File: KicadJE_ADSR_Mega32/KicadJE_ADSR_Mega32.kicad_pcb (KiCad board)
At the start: 2 copper layers, 100 x 100 mm, 217 parts, among them J101 ADSR1, J102 ADSR2, J103 ADSR1, J104 ADSR2, J105 ADSR1-G8, J106 ADSR2-G8, J107 ADSR4-G8, J108 ADSR3-G8, J201 AVR-ISP-6, J202 UART, J301 In, J302 +5V reg/doepfer, J303 Out, J304 CV_time, J305 CV doepfer, J401 CV, J402 FM, J403 Trigger, J404 Out, J405 SQ Out, J406 Sine Out, P101 Doepfer_Power_16pin, P302 Doepfer_Power_16pin, P401 Doepfer_Power_16pin, Q301 BC337, Q302 PZT2222A, Q401 UMX1N, Q402 MMBT2222A, Q403 MMBT2222A, Q404 MMBT2222A, Q405 MMBT2222A, SW401 LFO, SW402 SQ_Source, U201 ATmega32A-AU, U301 L78L05_TO92, U302 PT2399, U401 TL074, U402 74HC00, U403 TL072, Y201 16MHz

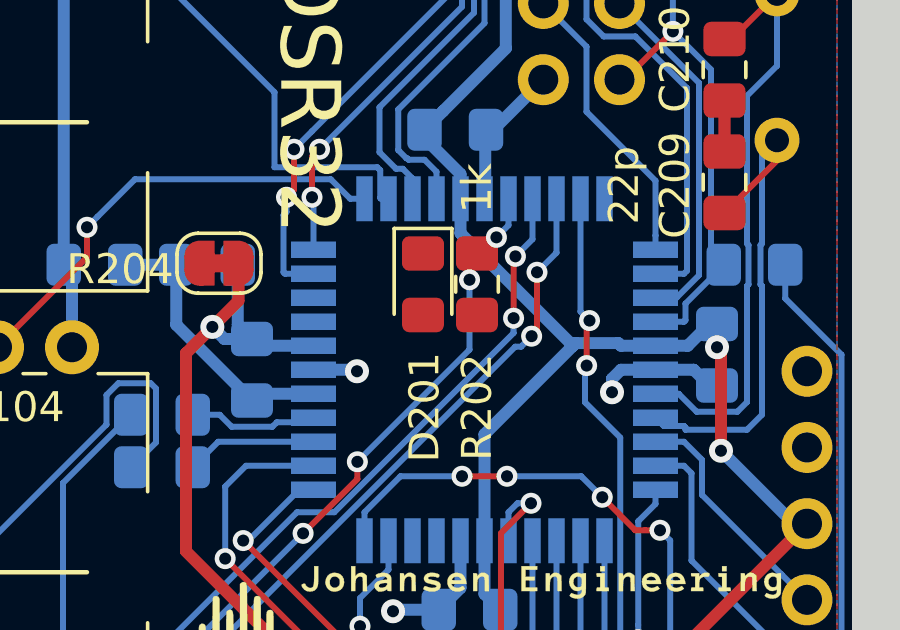
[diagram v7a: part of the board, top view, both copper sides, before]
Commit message: Arduino Blink
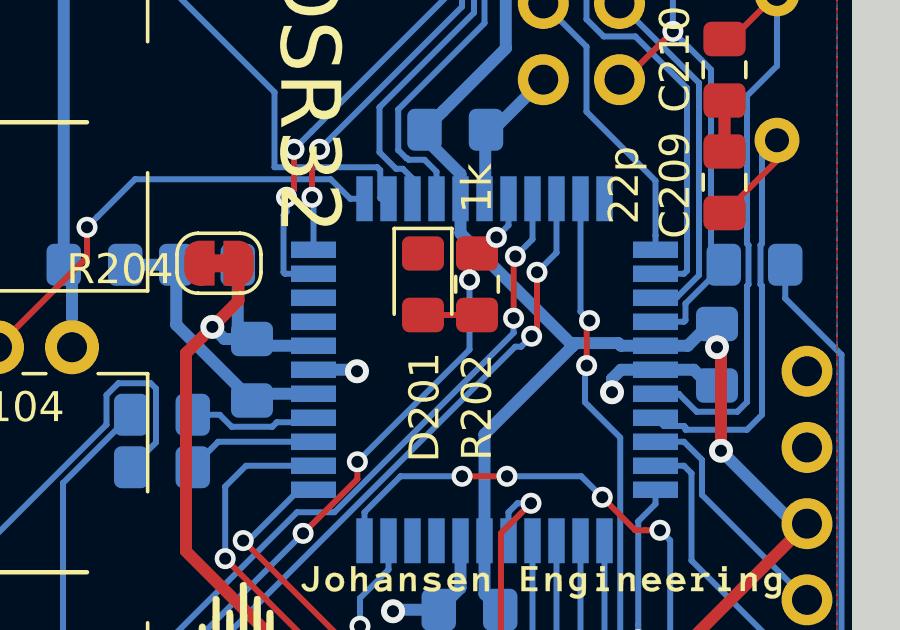
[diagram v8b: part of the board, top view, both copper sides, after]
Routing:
- net Net-(D201-Pad2): track 0.00 -> 1.80 mm
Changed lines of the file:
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@@
     (thickness 1.6)
     (drawings 38)
-    (tracks 1986)
+    (tracks 1987)
     (zones 0)
     (modules 217)
@@
   (page A4)
   (layers
-    (0 F.Cu signal)
+    (0 F.Cu signal hide)
     (31 B.Cu signal)
     (32 B.Adhes user hide)
@@
     (47 F.CrtYd user)
     (48 B.Fab user)
-    (49 F.Fab user hide)
+    (49 F.Fab user)
   )
   (setup
@@
   (segment (start 78.4 114.15001) (end 79.1 113.45001) (width 0.2) (layer B.Cu) (net 35))
   (segment (start 79.1 113.45001) (end 79.682115 113.45001) (width 0.2) (layer B.Cu) (net 35))
+  (segment (start 74.2 96.425) (end 76 96.425) (width 0.2) (layer F.Cu) (net 36))
   (segment (start 95.7 55) (end 96 54.7) (width 0.4) (layer F.Cu) (net 37))
   (segment (start 92.5 55) (end 95.7 55) (width 0.4) (layer F.Cu) (net 37) (status 10))
